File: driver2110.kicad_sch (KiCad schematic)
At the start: 40 parts, among them Q1 IRF840, Q2 IRF840, Q3 IRF840, Q4 IRF840, Q5 IRF840, Q6 IRF840, U3 IR2110, U6 IR2110, U9 IR2110

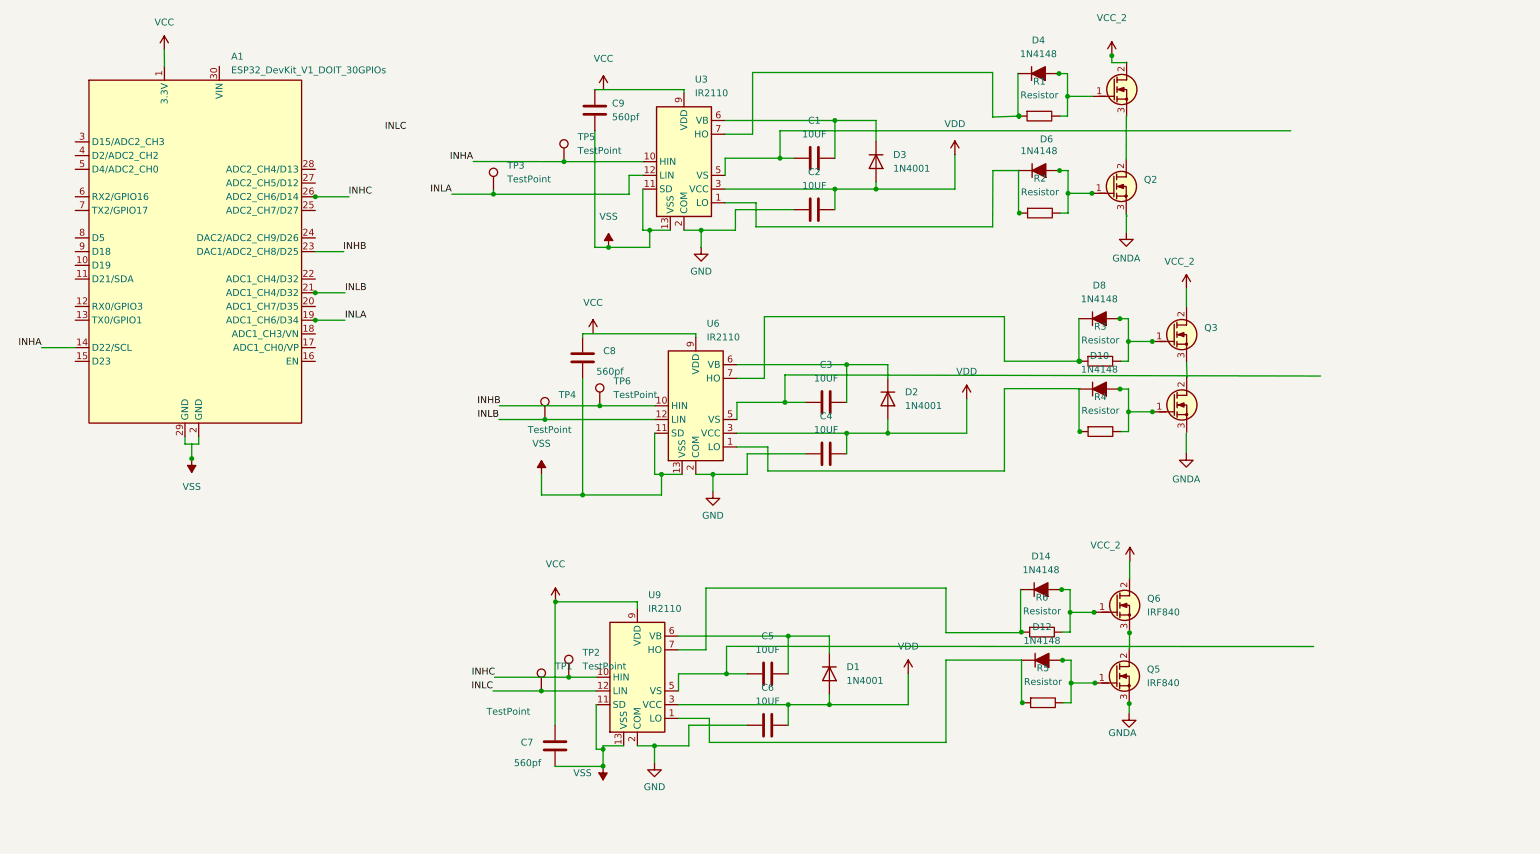
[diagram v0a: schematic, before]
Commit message: Correccion en la comprobacion del esquematico
para corregir los errores, se agregaron librerías, modificaron los cableados y se pusieron test points
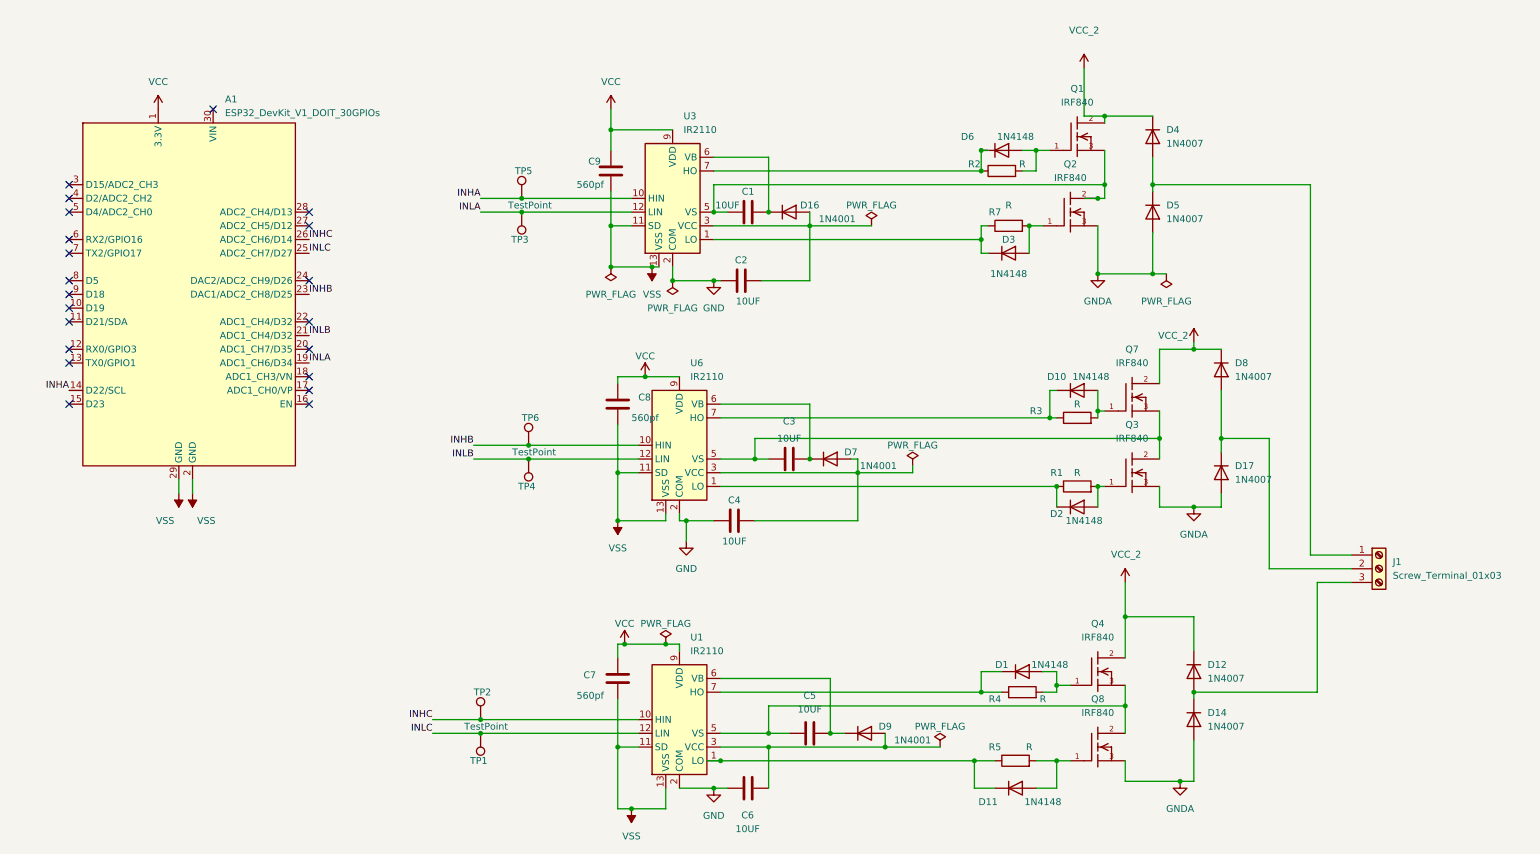
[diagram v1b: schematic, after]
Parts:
- removed D1, D2, D3: 1N4001, Diode_THT:D_DO-41_SOD81_P10.16mm_Horizontal, symbol Diode:1N4001
- removed D10, D12, D14, D4, D6, D8: 1N4148, Diode_THT_AKL:D_DO-35_SOD27_P7.62mm_Horizontal, symbol PCM_Diode_AKL:1N4148
- removed Q2, Q3, Q4, Q5, Q6: IRF840, Package_TO_SOT_THT_AKL:TO-220-3_Vertical_GDS, symbol PCM_Transistor_MOSFET_AKL:IRF840
- removed R1, R2, R3, R4, R5, R6: Resistor, Resistor_THT:R_Axial_DIN0207_L6.3mm_D2.5mm_P10.16mm_Horizontal, symbol PCM_SL_Devices:Resistor
- removed U9: IR2110, Package_DIP:DIP-14_W7.62mm, symbol Driver_FET:IR2110
- added D1, D10, D11, D2, D3, D6: 1N4148, Diode_THT:D_DO-35_SOD27_P7.62mm_Horizontal, symbol Diode:1N4148
- added D12, D14, D17, D4, D5, D8: 1N4007, Diode_THT:D_DO-41_SOD81_P10.16mm_Horizontal, symbol Diode:1N4007
- added D16, D7, D9: 1N4001, Diode_THT:D_DO-41_SOD81_P10.16mm_Horizontal, symbol Diode:1N4001
- added J1: Screw_Terminal_01x03, TerminalBlock:TerminalBlock_bornier-3_P5.08mm, symbol Connector:Screw_Terminal_01x03
- added Q2, Q3, Q4, Q7, Q8: IRF840, IRF840:TO220, symbol IRF840:IRF840
- added R1, R2, R3, R4, R5, R7: R, Resistor_THT:R_Axial_DIN0204_L3.6mm_D1.6mm_P1.90mm_Vertical, symbol Device:R
- added U1: IR2110, Package_DIP:DIP-14_W7.62mm, symbol Driver_FET:IR2110
- A1: footprint PCM_SL_Development_Boards:DOIT_ESP32_DEVKIT_30Pins -> ESP32-DEVKITC-32UE:ESPRESSIF_ESP32-DEVKITC-32UE
- Q1: footprint Package_TO_SOT_THT_AKL:TO-220-3_Vertical_GDS -> IRF840:TO220; symbol PCM_Transistor_MOSFET_AKL:IRF840 -> IRF840:IRF840; Availability (none) -> In Stock; Check_prices (none) -> https://www.snapeda.com/parts/IRF840/Vishay+Siliconix/view-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; MF (none) -> Vishay; MP (none) -> IRF840; Package (none) -> TO-220-3 Vishay; Price (none) -> None; SnapEDA_Link (none) -> https://www.snapeda.com/parts/IRF840/Vishay+Siliconix/view-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
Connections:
- net GND: now also U1.2 (COM)
- net INHC: now also A1.26 (ADC2_CH6/D14), U1.10 (HIN)
- net INLC: now also A1.25 (ADC2_CH7/D27), U1.12 (LIN)
- net VCC: now also A1.1 (3.3V), C8.1, C9.1, Q1.2, U3.9 (VDD), U6.9 (VDD), D12.1 (K), D4.1 (K), D8.1 (K), Q4.2, Q7.2, U1.9 (VDD)
- net VSS: now also A1.2 (GND), A1.29 (GND), U1.11 (SD), U1.13 (VSS)
- net at C5.2: now also D9.1 (K), U1.6 (VB)
- net at U3.1 (LO): now also D3.1 (K), R7.1
- net at Q1.1: now also D6.2 (A), R2.2
- net at Q1.3: now also C1.1, U3.5 (VS), Q2.2
- net at U3.7 (HO): now also D6.1 (K), R2.1
- net at C3.2, U6.6 (VB): now also D7.1 (K)
- net at C1.2, U3.6 (VB): now also D16.1 (K)
- net at U6.7 (HO): now also D10.1 (K), R3.1
- net at C5.1: now also Q4.3, Q8.2, U1.5 (VS)
- net at U6.1 (LO): now also D2.1 (K), R1.1
- net at C3.1, U6.5 (VS): now also Q3.2, Q7.3
- removed net VDD: C2.2, C4.2, C6.2, U3.3 (VCC), U6.3 (VCC)
- new net: D10.2 (A), Q7.1, R3.2
- new net: D4.2 (A), D5.1 (K), J1.1 (Pin_1)
- new net: C4.2, D7.2 (A), U6.3 (VCC)
- new net: C2.2, D16.2 (A), U3.3 (VCC)
- new net: D17.1 (K), D8.2 (A), J1.2 (Pin_2)
- new net: D12.2 (A), D14.1 (K), J1.3 (Pin_3)
- new net: C6.2, D9.2 (A), U1.3 (VCC)
- new net: D2.2 (A), Q3.1, R1.2
- new net: D11.2 (A), Q8.1, R5.2
- new net: D11.1 (K), R5.1, U1.1 (LO)
- new net: D1.1 (K), R4.1, U1.7 (HO)
- new net: D1.2 (A), Q4.1, R4.2
- new net: D3.2 (A), Q2.1, R7.2
- new net GNDA: D14.2 (A), D17.2 (A), D5.2 (A), Q2.3, Q3.3, Q8.3
- no-connect marks 0 -> 21
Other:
- moved on the sheet: A1, C1, C2, C3, C4, C5, C6, C7, C8, C9, TP1, TP2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
